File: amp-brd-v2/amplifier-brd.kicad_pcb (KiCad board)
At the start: 2 copper layers, 32.5 x 30 mm, 23 parts, among them J1 VOUT, U1 OPA547F, U2 INA233

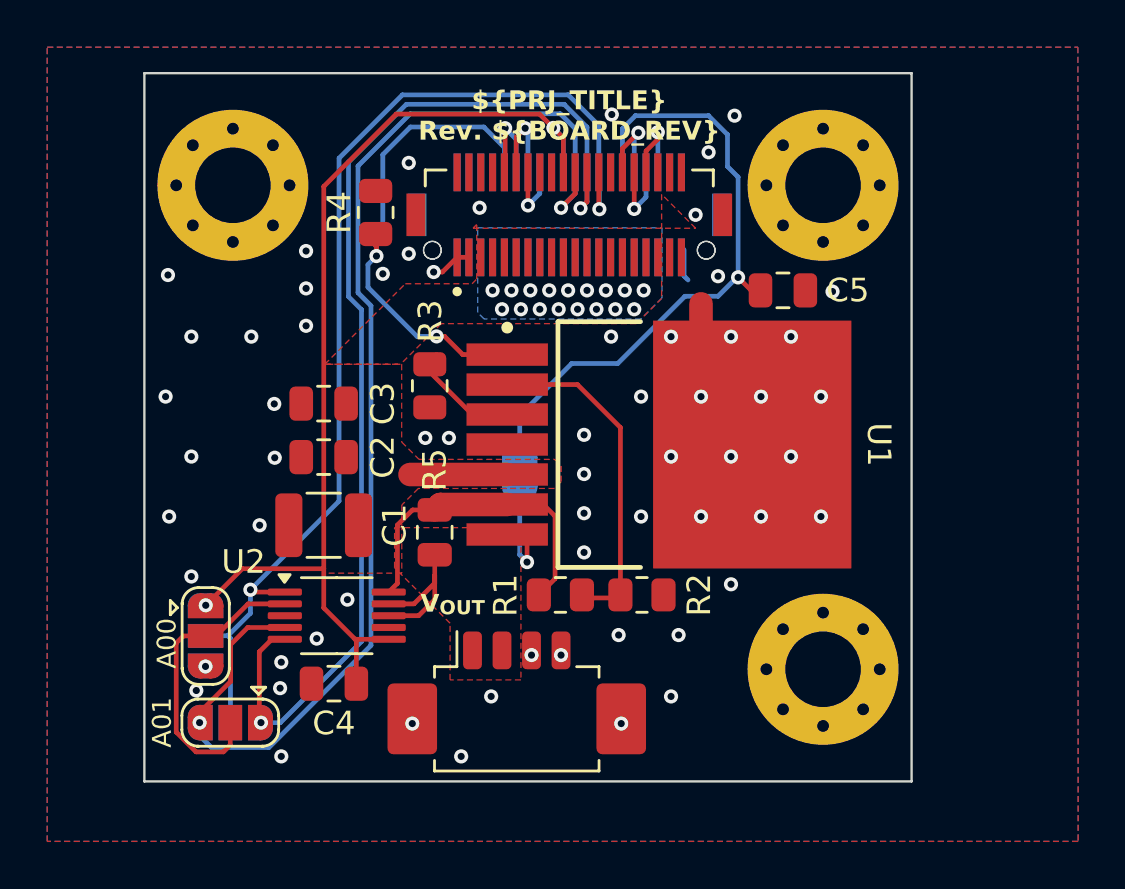
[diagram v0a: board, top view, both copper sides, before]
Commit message: Added onewire temperature sensor
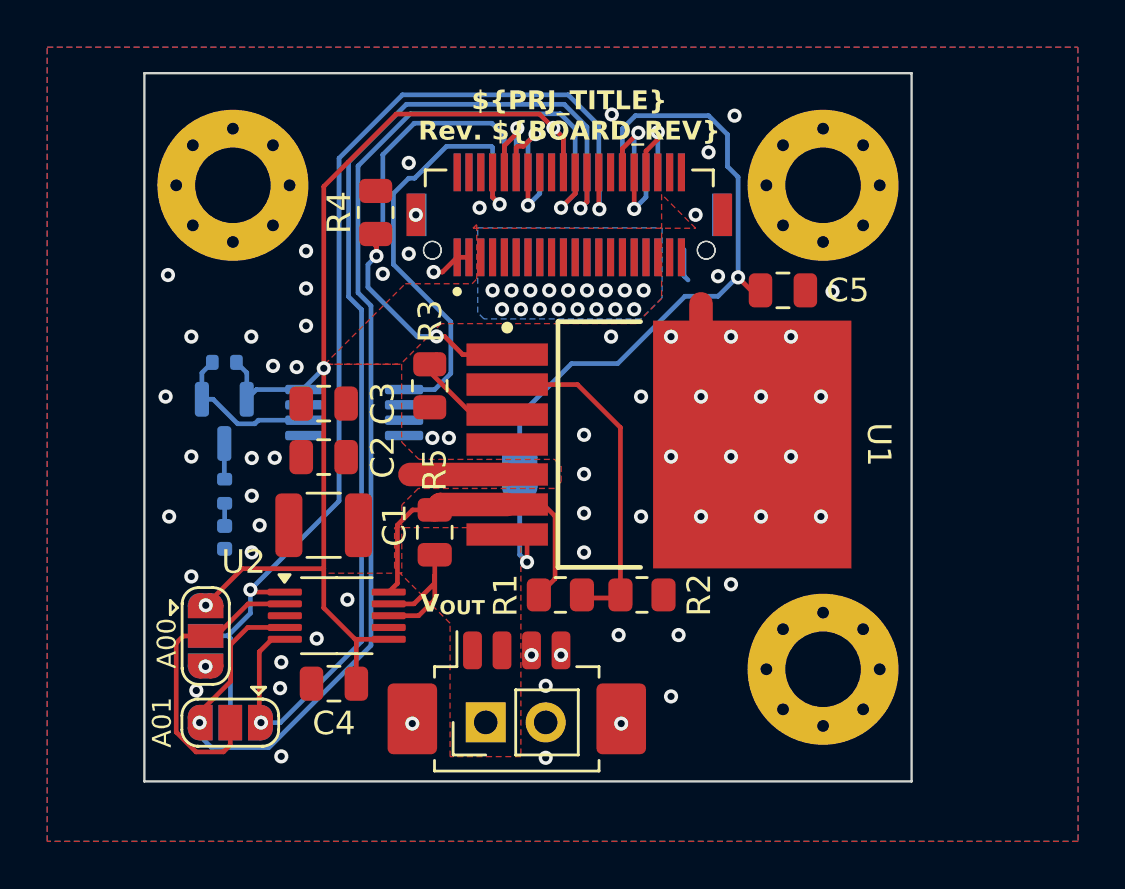
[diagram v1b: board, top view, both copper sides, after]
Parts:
- added D1: LED, LED_SMD:LED_0402_1005Metric, B.Cu at (216.3, 103.7)
- added J2: VOUT, Connector_PinHeader_2.54mm:PinHeader_1x02_P2.54mm_Vertical, F.Cu at (227.4, 111.6)
- added Q1: BSS84, Package_TO_SOT_SMD:SOT-23, B.Cu at (216.3, 98.8)
- added R6: 1k, Resistor_SMD:R_0402_1005Metric, B.Cu at (216.3, 101.8)
- added R7: 10k, Resistor_SMD:R_0402_1005Metric, B.Cu at (216.3, 96.3)
- added U3: DS28EA00, Package_SO:MSOP-8_3x3mm_P0.65mm, B.Cu at (221.8, 98.4)
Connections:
- BOT1 pad 37: GND -> /ONEWIRE
- TOP1 pad 37: GND -> /ONEWIRE
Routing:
- net /ONEWIRE: track 0.00 -> 19.9 mm, vias 0 -> 1
- net Net-(Q1-G): track 0.00 -> 6.58 mm
- net +3V3: track 44.1 -> 49.7 mm, vias 2 -> 3
- net Net-(Q1-D): track 0.00 -> 1.52 mm
- net Net-(D1-A): track 0.00 -> 0.96 mm
- net GND: vias 62 -> 67

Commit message: Added FB smoothing capacitor to amp brd
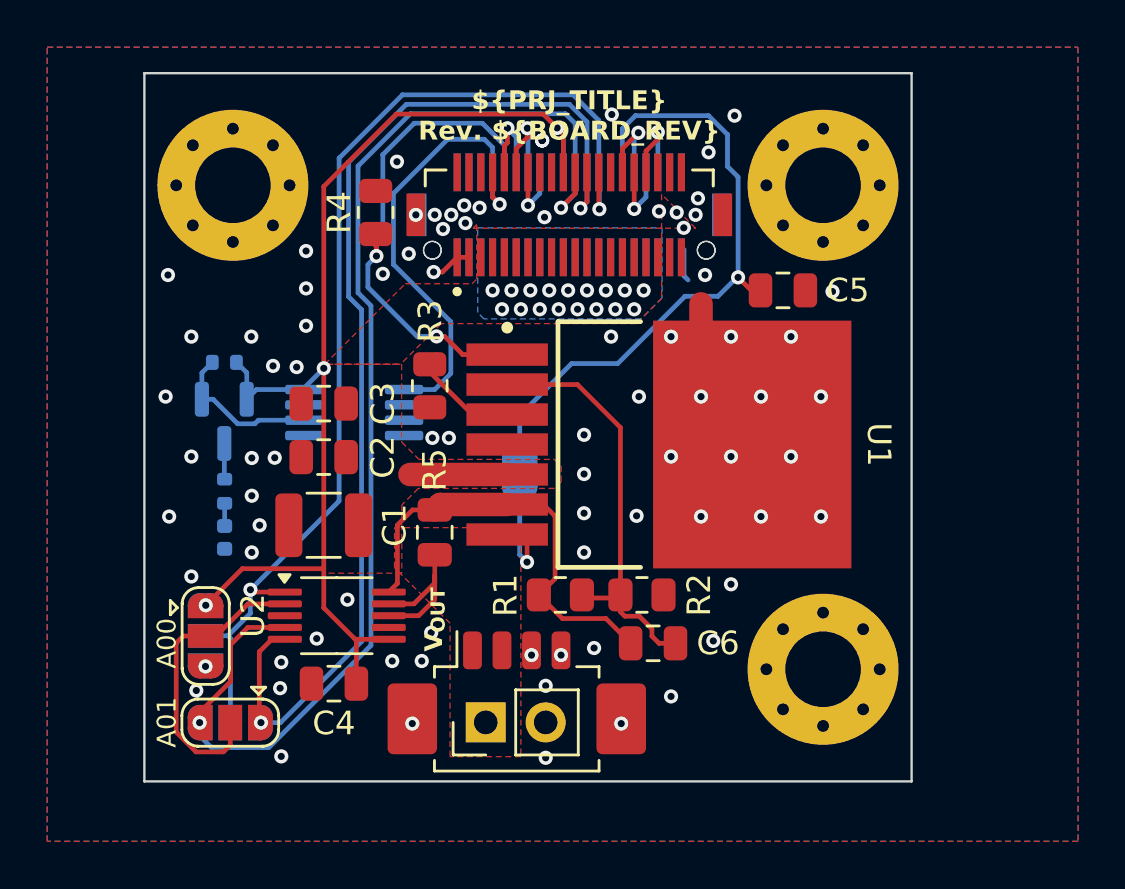
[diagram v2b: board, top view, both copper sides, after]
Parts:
- added C6: 0.01u, Capacitor_SMD:C_0805_2012Metric, F.Cu at (234.4, 108.2)
- A00, A01: value SolderJumper_3_Open -> L / NC / R
- A10, A11: value SolderJumper_3_Open -> NC
- U1: value OPA547F -> OPA548
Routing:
- net /OP AMP/V_{RAW}: track 13.9 -> 18.6 mm
- net /OP AMP/OP_FB: track 14.3 -> 18.1 mm
- net GND: vias 67 -> 82
- added copper zone on In1.Cu, net GND
- added copper zone on In2.Cu, net GND
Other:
- copper layers 2 -> 4
- board text added: "0"
- board text added: "0 mm"
- board text added: "0.0000 mm / 0.0000 mm"
- board text added: "0.01 mm"
- board text added: "0.02"
- board text added: "0.035 mm"
- board text added: "0.1 mm"
- board text added: "0.3000 mm"
- board text added: "1"
- board text added: "1.24 mm"
- board text added: "1.6000 mm"
- board text added: "3.3"
- board text added: "32.5000 mm x 30.0000 mm"
- board text added: "4"
- board text added: "4.5"
- board text added: "B.Cu"
- board text added: "B.Mask"
- board text added: "B.Paste"
- board text added: "B.Silkscreen"
- board text added: "BOARD CHARACTERISTICS"
- board text added: "Board Thickness:"
- board text added: "Board overall dimensions:"
- board text added: "Bottom Silk Screen"
- board text added: "Bottom Solder Mask"
- board text added: "Bottom Solder Paste"
- board text added: "Castellated pads:"
- board text added: "Color"
- board text added: "Copper Finish:"
- board text added: "Copper Layer Count:"
- board text added: "Designer: ${DESIGNER} Reviewer: ${REVIEWER}"
- board text added: "Dielectric"
- board text added: "Edge card connectors:"
- board text added: "Epsilon R"
- board text added: "F.Cu"
- board text added: "F.Mask"
- board text added: "F.Paste"
- board text added: "F.Silkscreen"
- board text added: "FR4"
- board text added: "Impedance Control:"
- board text added: "In1.Cu"
- board text added: "In2.Cu"
- board text added: "Layer Name"
- board text added: "Loss Tangent"
- board text added: "Material"
- board text added: "Min hole diameter:"
- board text added: "Min track/spacing:"
- board text added: "No"
- board text added: "None"
- board text added: "Not specified"
- board text added: "Plated Board Edge:"
- board text added: "Thickness (mm)"
- board text added: "Top Silk Screen"
- board text added: "Top Solder Mask"
- board text added: "Top Solder Paste"
- board text added: "Type"
- board text added: "copper"
- board text added: "core"
- board text added: "prepreg"

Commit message: Modified DAC, AMP v2 and Mezzanine to support AMP v3. Finished AMP v3 design.
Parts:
- R1: value 10k -> 13k
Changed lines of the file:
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@@
 			)
 		)
-		(property "Value" "10k"
+		(property "Value" "13k"
 			(at 2.6725 0 0)
 			(layer "F.Fab")
@@
 			)
 		)
-		(property "Datasheet" "https://www.mouser.com/datasheet/3/317/1/ASC_WFxxP.pdf"
+		(property "Datasheet" "https://www.te.com/commerce/DocumentDelivery/DDEController?Action=srchrtrv&DocNm=1623112&DocType=Customer+Drawing&DocLang=English&PartCntxt=1623112-1"
 			(at 0 0 0)
 			(layer "F.Fab")
@@
 			)
 		)
-		(property "Description" "Thin Film Resistors 10K Ohms 250mW +/- 1% 0805"
+		(property "Description" "Thick Film Resistors CRG0805 1% 13K"
 			(at 0 0 0)
 			(layer "F.Fab")
@@
 			)
 		)
-		(property "Mfr" "Walsin"
+		(property "Mfr" "TE Connectivity / Holsworthy "
 			(at 0 0 180)
 			(unlocked yes)
@@
 			)
 		)
-		(property "Mfr #" "WF08P1002FTL"
+		(property "Mfr #" "CRG0805F13K"
 			(at 0 0 180)
 			(unlocked yes)
@@
 			)
 		)
-		(property "Mouser #" "791-WF08P1002FTL"
+		(property "Mouser #" "279-CRG0805F13K"
 			(at 0 0 180)
 			(unlocked yes)
@@
 			)
 		)
-		(property "Mouser URL" "https://www.mouser.com/ProductDetail/Walsin/WF08P1002FTL?qs=sGAEpiMZZMvdGkrng054t7z4BkURc4LzCx%252B5OuE3qppREPl7ULZTTA%3D%3D"
+		(property "Mouser URL" "https://www.mouser.com/ProductDetail/TE-Connectivity-Holsworthy/CRG0805F13K?qs=sGAEpiMZZMvdGkrng054t%252BGQy31YLTNMxyRamAR5vSg%3D"
 			(at 0 0 180)
 			(unlocked yes)

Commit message: Optimized temperature sensor from Kuravi's design, reworked inductor placement in amp board v3
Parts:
- R7: value 10k -> 100k
